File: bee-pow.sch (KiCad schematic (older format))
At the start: 4 parts, among them J1 Conn_01x02_Male, J2 Conn_01x02_Male, J3 Conn_01x02_Male, J4 Conn_01x02_Male

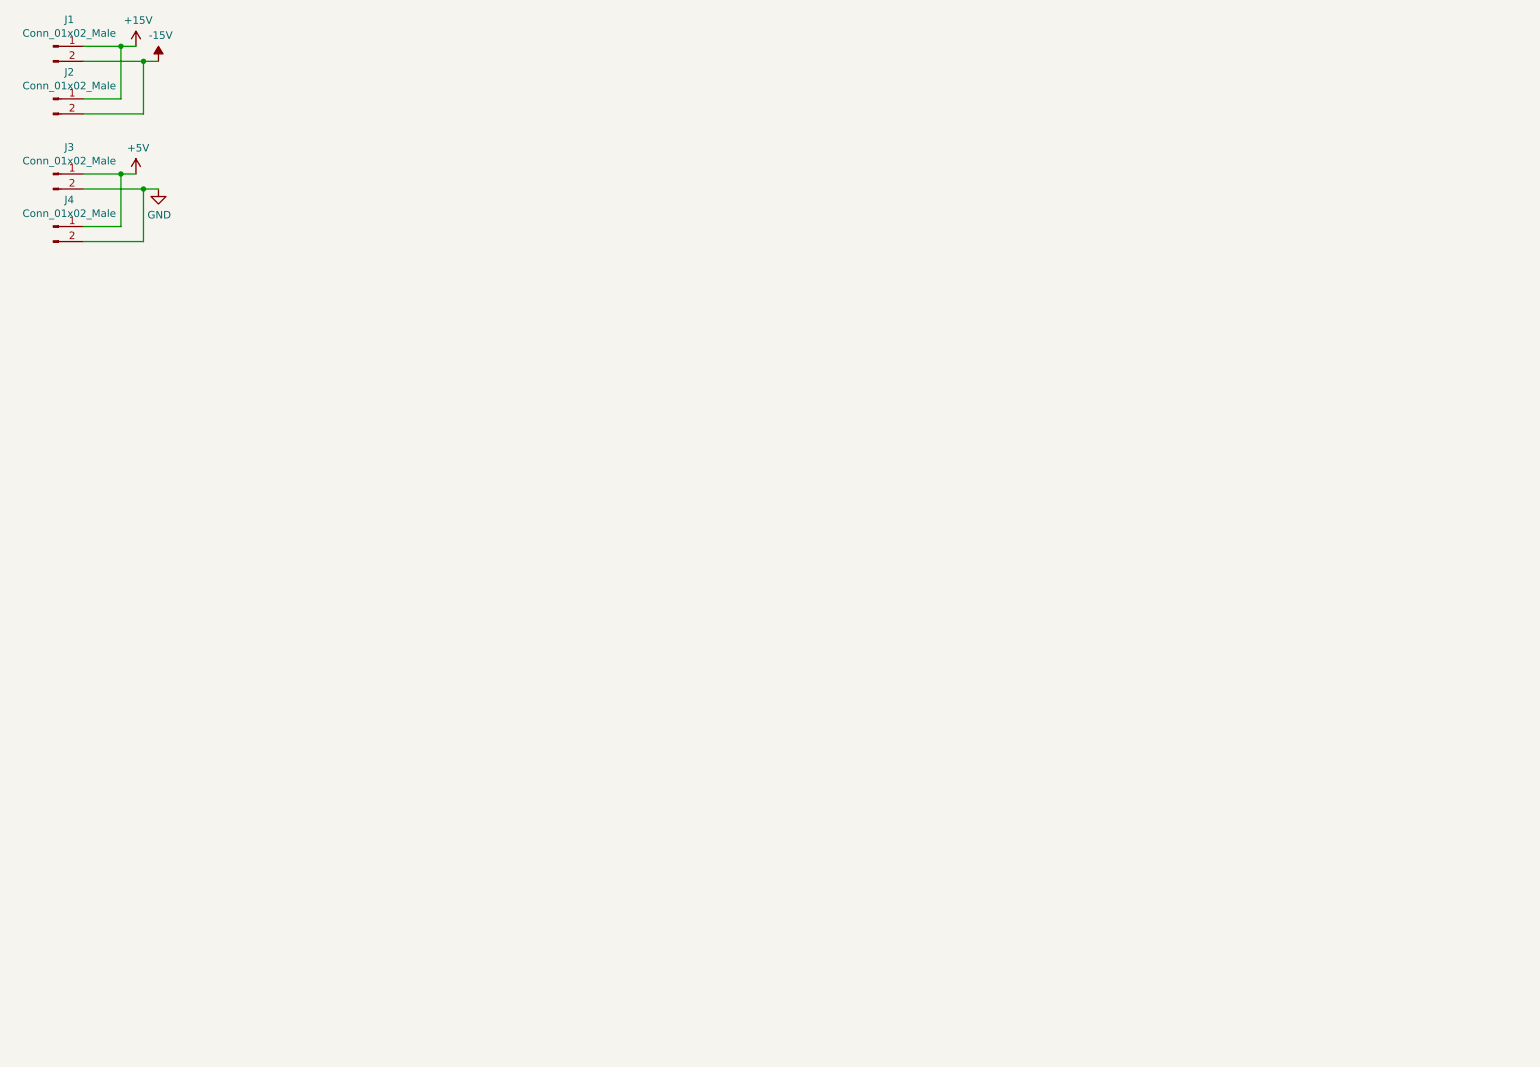
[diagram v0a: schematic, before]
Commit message: begin schematic
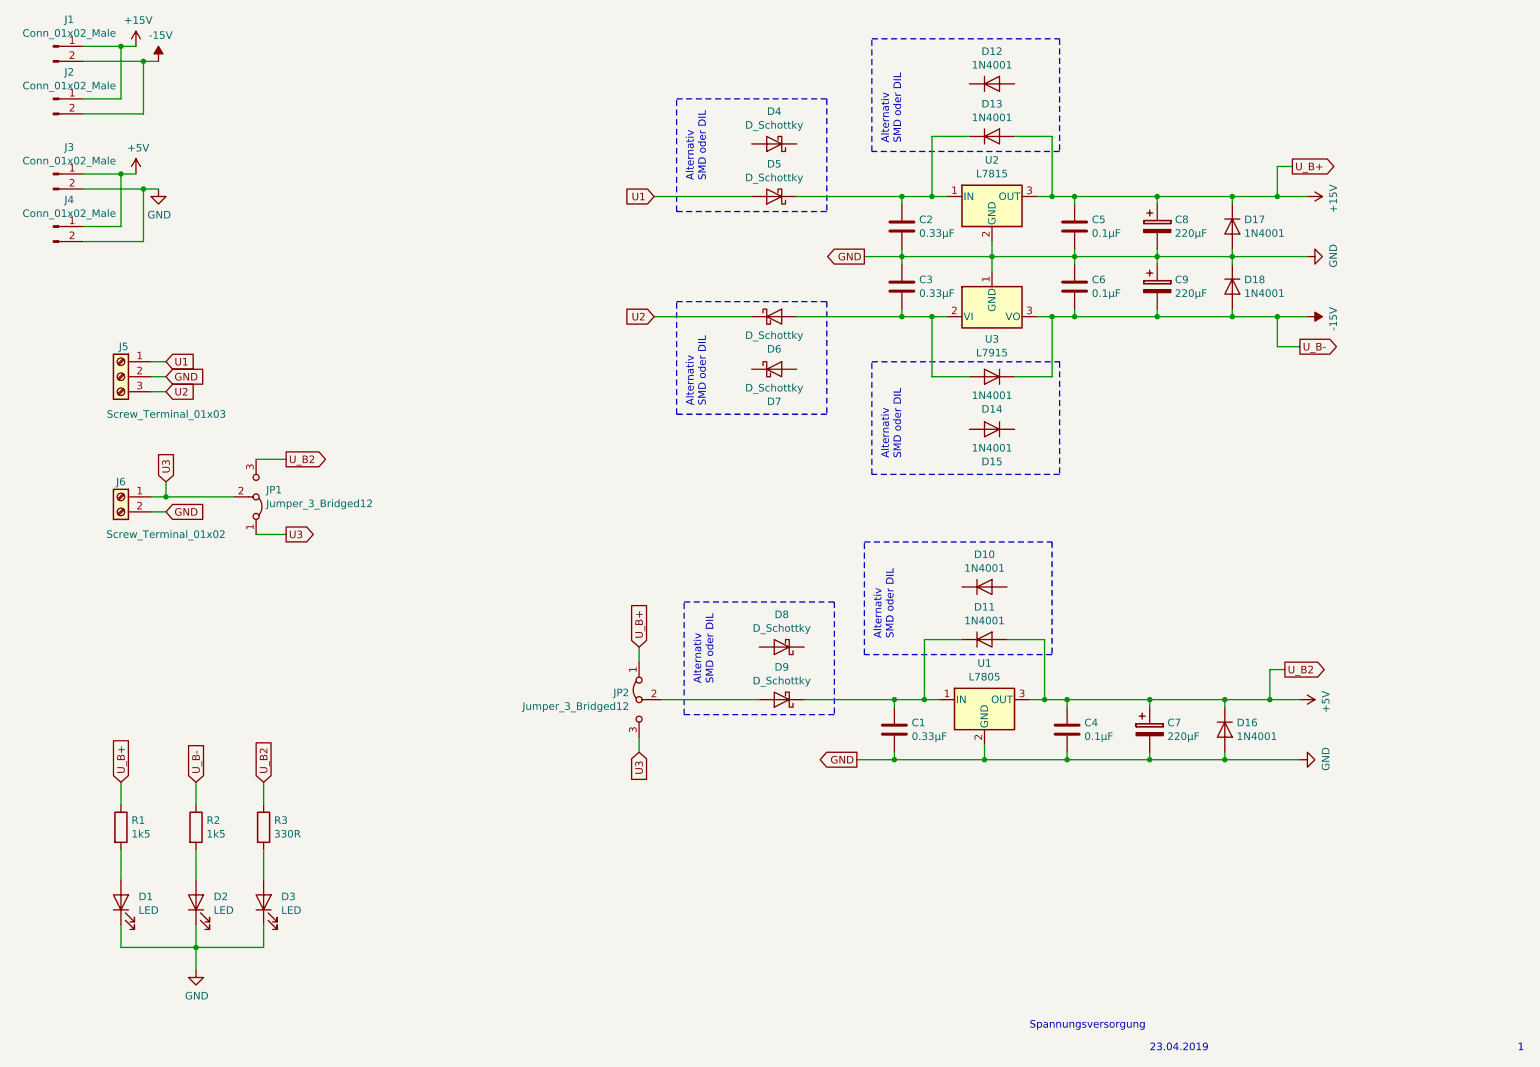
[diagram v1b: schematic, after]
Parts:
- added C1, C2, C3: 0.33µF, Capacitor_SMD:C_0805_2012Metric_Pad1.15x1.40mm_HandSolder, symbol Device:C
- added C4, C5, C6: 0.1µF, Capacitor_SMD:C_0805_2012Metric_Pad1.15x1.40mm_HandSolder, symbol Device:C
- added C7, C8, C9: 220µF, Capacitor_THT:CP_Radial_D10.0mm_P5.00mm, symbol Device:CP
- added D1, D2, D3: LED, LED_SMD:LED_0805_2012Metric_Pad1.15x1.40mm_HandSolder, symbol Device:LED
- added D10, D12, D15: 1N4001, Diode_THT:D_A-405_P12.70mm_Horizontal, symbol Diode:1N4001
- added D11, D13, D14, D16, D17, D18: 1N4001, Diode_SMD:D_MELF_Handsoldering, symbol Diode:1N4001
- added D4, D7, D8: D_Schottky, Diode_THT:D_A-405_P10.16mm_Horizontal, symbol Device:D_Schottky
- added D5, D6, D9: D_Schottky, Diode_SMD:D_SMB, symbol Device:D_Schottky
- added J5: Screw_Terminal_01x03, TerminalBlock:TerminalBlock_bornier-3_P5.08mm, symbol Connector:Screw_Terminal_01x03
- added J6: Screw_Terminal_01x02, TerminalBlock:TerminalBlock_bornier-2_P5.08mm, symbol Connector:Screw_Terminal_01x02
- added JP1, JP2: Jumper_3_Bridged12, Connector_PinHeader_2.54mm:PinHeader_1x03_P2.54mm_Vertical, symbol Jumper:Jumper_3_Bridged12
- added R1, R2: 1k5, Resistor_SMD:R_0805_2012Metric_Pad1.15x1.40mm_HandSolder, symbol Device:R
- added R3: 330R, Resistor_SMD:R_0805_2012Metric_Pad1.15x1.40mm_HandSolder, symbol Device:R
- added U1: L7805, Package_TO_SOT_THT:TO-220-3_Vertical, symbol Regulator_Linear:L7805
- added U2: L7815, Package_TO_SOT_THT:TO-220-3_Vertical, symbol Regulator_Linear:L7815
- added U3: L7915, Package_TO_SOT_THT:TO-220-3_Vertical, symbol Regulator_Linear:L7915
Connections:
- net +15V: now also C5.1, C8.1, D13.2 (A), D17.1 (K), JP2.1 (A), R1.1, U2.3 (OUT)
- net +5V: now also C4.1, C7.1, D11.2 (A), D16.1 (K), JP1.3 (B), R3.1, U1.3 (OUT)
- net -15V: now also C6.2, C9.2, D14.1 (K), D18.2 (A), R2.1, U3.3 (VO)
- net GND: now also C1.2, C2.2, C3.1, C4.2, C5.2, C6.1, C7.2, C8.2, C9.1, D1.1 (K), D16.2 (A), D17.2 (A), D18.1 (K), D2.1 (K), D3.1 (K), J5.2 (Pin_2), J6.2 (Pin_2), U1.2 (GND), U2.2 (GND), U3.1 (GND)
- new net: C2.1, D13.1 (K), D5.1 (K), U2.1 (IN)
- new net: C3.2, D14.2 (A), D6.2 (A), U3.2 (VI)
- new net: D9.2 (A), JP2.2 (C)
- new net: C1.1, D11.1 (K), D9.1 (K), U1.1 (IN)
- new net: D1.2 (A), R1.2
- new net: D2.2 (A), R2.2
- new net: D3.2 (A), R3.2
- new net U1: D5.2 (A), J5.1 (Pin_1)
- new net U2: D6.1 (K), J5.3 (Pin_3)
- new net U3: J6.1 (Pin_1), JP1.1 (A), JP1.2 (C), JP2.3 (B)
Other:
- note added: "1"
- note added: "23.04.2019"
- note added: "Alternativ \nSMD oder DIL"
- note added: "Spannungsversorgung"
